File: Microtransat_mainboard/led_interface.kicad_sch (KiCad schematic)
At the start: 12 parts, among them J8 Conn_01x07

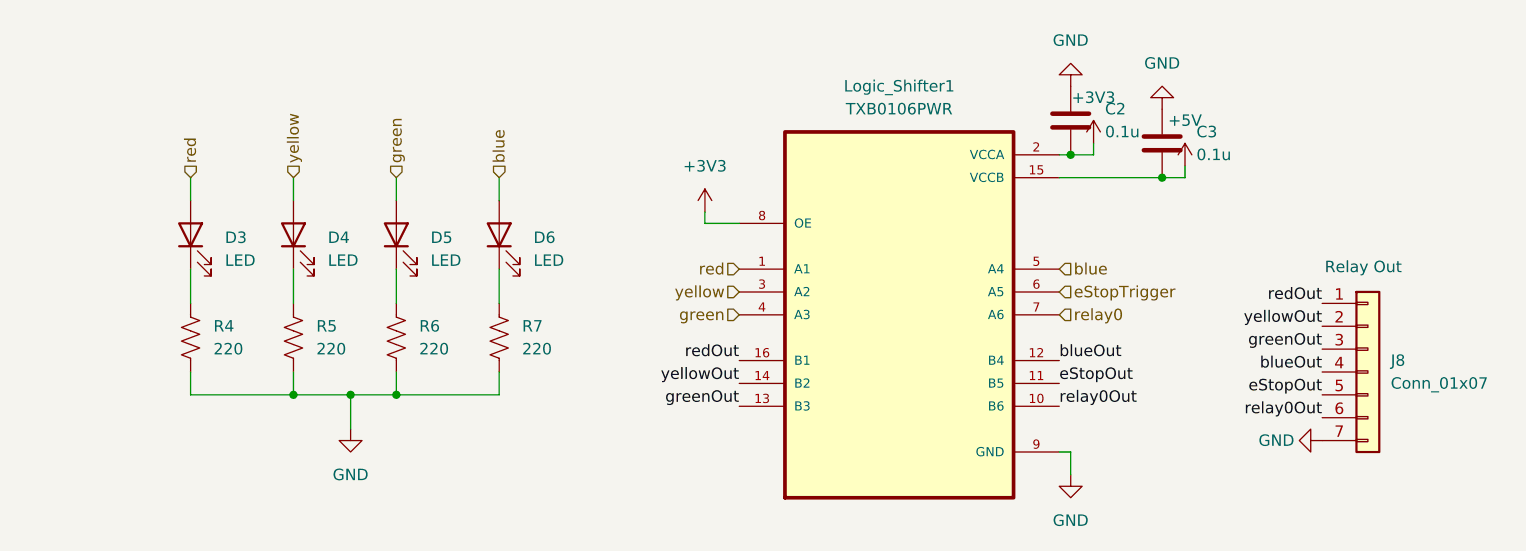
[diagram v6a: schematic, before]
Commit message: Some small changes to silkscreen and component numbers
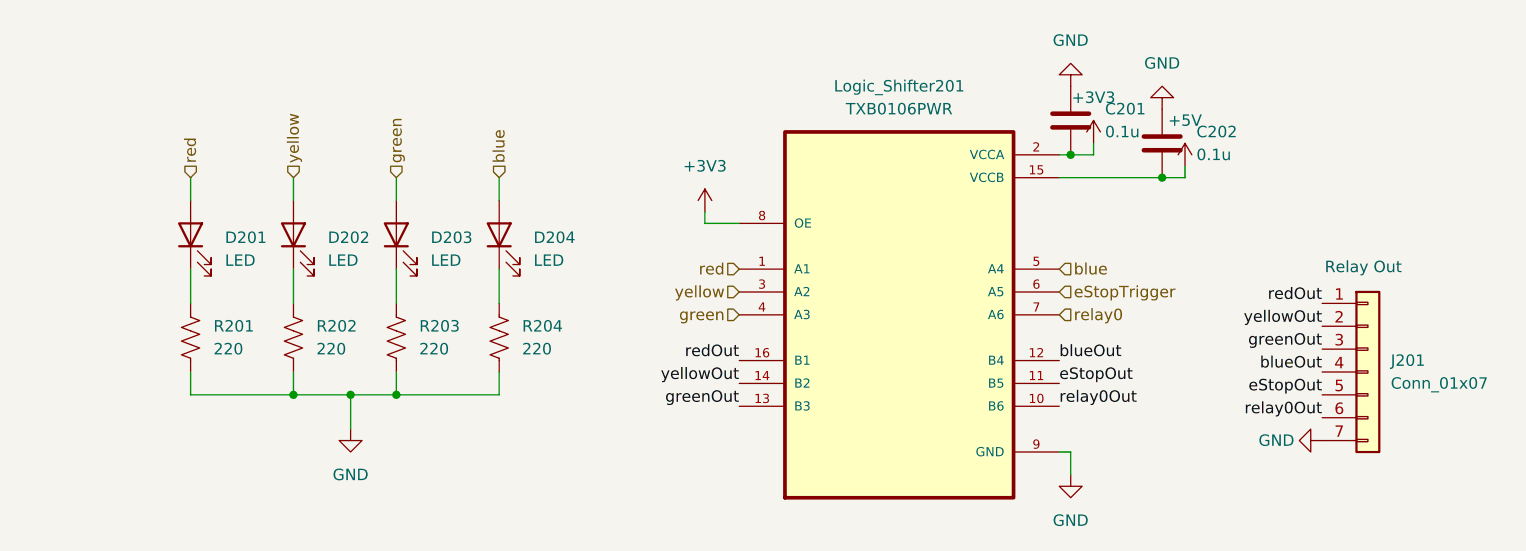
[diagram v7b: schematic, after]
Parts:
- renumbered C2 to C201, C3 to C202, D3 to D201, D4 to D202, D5 to D203, D6 to D204, J8 to J201, Logic_Shifter1 to Logic_Shifter201, R4 to R201, R5 to R202, R6 to R203, R7 to R204
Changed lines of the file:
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@@
 		(dnp no)
 		(fields_autoplaced yes)
-		(property "Reference" "R6"
+		(property "Reference" "R203"
 			(at 93.98 81.2799 0)
 			(effects
@@
 			(project "Microtransat_mainboard"
 				(path "/89914625-be83-416e-bb0d-b792f59b4aa6/2a723dab-0fe3-42a5-a32e-d625b3338ba9"
-					(reference "R6")
+					(reference "R203")
 					(unit 1)
 				)
@@
 		(dnp no)
 		(fields_autoplaced yes)
-		(property "Reference" "R4"
+		(property "Reference" "R201"
 			(at 71.12 81.2799 0)
 			(effects
@@
 			(project "Microtransat_mainboard"
 				(path "/89914625-be83-416e-bb0d-b792f59b4aa6/2a723dab-0fe3-42a5-a32e-d625b3338ba9"
-					(reference "R4")
+					(reference "R201")
 					(unit 1)
 				)
@@
 		(dnp no)
 		(fields_autoplaced yes)
-		(property "Reference" "#PWR031"
+		(property "Reference" "#PWR0205"
 			(at 168.91 64.77 0)
 			(effects
@@
 			(project "Microtransat_mainboard"
 				(path "/89914625-be83-416e-bb0d-b792f59b4aa6/2a723dab-0fe3-42a5-a32e-d625b3338ba9"
-					(reference "#PWR031")
+					(reference "#PWR0205")
 					(unit 1)
 				)
@@
 		(dnp no)
 		(fields_autoplaced yes)
-		(property "Reference" "R7"
+		(property "Reference" "R204"
 			(at 105.41 81.2799 0)
 			(effects
@@
 			(project "Microtransat_mainboard"
 				(path "/89914625-be83-416e-bb0d-b792f59b4aa6/2a723dab-0fe3-42a5-a32e-d625b3338ba9"
-					(reference "R7")
+					(reference "R204")
 					(unit 1)
 				)
@@
 		(dnp no)
 		(fields_autoplaced yes)
-		(property "Reference" "D4"
+		(property "Reference" "D202"
 			(at 83.82 71.4374 90)
 			(effects
@@
 			(project "Microtransat_mainboard"
 				(path "/89914625-be83-416e-bb0d-b792f59b4aa6/2a723dab-0fe3-42a5-a32e-d625b3338ba9"
-					(reference "D4")
+					(reference "D202")
 					(unit 1)
 				)
@@
 		(dnp no)
 		(fields_autoplaced yes)
-		(property "Reference" "#PWR033"
+		(property "Reference" "#PWR0207"
 			(at 179.07 67.31 0)
 			(effects
@@
 			(project "Microtransat_mainboard"
 				(path "/89914625-be83-416e-bb0d-b792f59b4aa6/2a723dab-0fe3-42a5-a32e-d625b3338ba9"
-					(reference "#PWR033")
+					(reference "#PWR0207")
 					(unit 1)
 				)
@@
 		(dnp no)
 		(fields_autoplaced yes)
-		(property "Reference" "J8"
+		(property "Reference" "J201"
 			(at 201.93 85.0899 0)
 			(effects
@@
 			(project ""
 				(path "/89914625-be83-416e-bb0d-b792f59b4aa6/2a723dab-0fe3-42a5-a32e-d625b3338ba9"
-					(reference "J8")
+					(reference "J201")
 					(unit 1)
 				)
@@
 		(dnp no)
 		(fields_autoplaced yes)
-		(property "Reference" "D6"
+		(property "Reference" "D204"
 			(at 106.68 71.4374 90)
 			(effects
@@
 			(project "Microtransat_mainboard"
 				(path "/89914625-be83-416e-bb0d-b792f59b4aa6/2a723dab-0fe3-42a5-a32e-d625b3338ba9"
-					(reference "D6")
+					(reference "D204")
 					(unit 1)
 				)
@@
 		(dnp no)
 		(fields_autoplaced yes)
-		(property "Reference" "#PWR029"
+		(property "Reference" "#PWR0203"
 			(at 166.37 48.26 0)
 			(effects
@@
 			(project "Microtransat_mainboard"
 				(path "/89914625-be83-416e-bb0d-b792f59b4aa6/2a723dab-0fe3-42a5-a32e-d625b3338ba9"
-					(reference "#PWR029")
+					(reference "#PWR0203")
 					(unit 1)
 				)
@@
 		(dnp no)
 		(fields_autoplaced yes)
-		(property "Reference" "#PWR030"
+		(property "Reference" "#PWR0204"
 			(at 166.37 104.14 0)
 			(effects
@@
 			(project "Microtransat_mainboard"
 				(path "/89914625-be83-416e-bb0d-b792f59b4aa6/2a723dab-0fe3-42a5-a32e-d625b3338ba9"
-					(reference "#PWR030")
+					(reference "#PWR0204")
 					(unit 1)
 				)
@@
 		(dnp no)
 		(fields_autoplaced yes)
-		(property "Reference" "#PWR032"
+		(property "Reference" "#PWR0206"
 			(at 176.53 50.8 0)
 			(effects
@@
 			(project "Microtransat_mainboard"
 				(path "/89914625-be83-416e-bb0d-b792f59b4aa6/2a723dab-0fe3-42a5-a32e-d625b3338ba9"
-					(reference "#PWR032")
+					(reference "#PWR0206")
 					(unit 1)
 				)
@@
 		(dnp no)
 		(fields_autoplaced yes)
-		(property "Reference" "D5"
+		(property "Reference" "D203"
 			(at 95.25 71.4374 90)
 			(effects
@@
 			(project "Microtransat_mainboard"
 				(path "/89914625-be83-416e-bb0d-b792f59b4aa6/2a723dab-0fe3-42a5-a32e-d625b3338ba9"
-					(reference "D5")
+					(reference "D203")
 					(unit 1)
 				)
@@
 		(dnp no)
 		(fields_autoplaced yes)
-		(property "Reference" "D3"
+		(property "Reference" "D201"
 			(at 72.39 71.4374 90)
 			(effects
@@
 			(project "Microtransat_mainboard"
 				(path "/89914625-be83-416e-bb0d-b792f59b4aa6/2a723dab-0fe3-42a5-a32e-d625b3338ba9"
-					(reference "D3")
+					(reference "D201")
 					(unit 1)
 				)
@@
 		(dnp no)
 		(fields_autoplaced yes)
-		(property "Reference" "#PWR027"
+		(property "Reference" "#PWR0201"
 			(at 86.36 99.06 0)
 			(effects
@@
 			(project "Microtransat_mainboard"
 				(path "/89914625-be83-416e-bb0d-b792f59b4aa6/2a723dab-0fe3-42a5-a32e-d625b3338ba9"
-					(reference "#PWR027")
+					(reference "#PWR0201")
 					(unit 1)
 				)
@@
 		(dnp no)
 		(fields_autoplaced yes)
-		(property "Reference" "Logic_Shifter1"
+		(property "Reference" "Logic_Shifter201"
 			(at 147.32 54.61 0)
 			(effects
@@
 			(project "Microtransat_mainboard"
 				(path "/89914625-be83-416e-bb0d-b792f59b4aa6/2a723dab-0fe3-42a5-a32e-d625b3338ba9"
-					(reference "Logic_Shifter1")
+					(reference "Logic_Shifter201")
 					(unit 1)
 				)
@@
 		(dnp no)
 		(fields_autoplaced yes)
-		(property "Reference" "C2"
+		(property "Reference" "C201"
 			(at 170.18 57.1499 0)
 			(effects
@@
 			(project ""
 				(path "/89914625-be83-416e-bb0d-b792f59b4aa6/2a723dab-0fe3-42a5-a32e-d625b3338ba9"
-					(reference "C2")
+					(reference "C201")
 					(unit 1)
 				)
@@
 		(dnp no)
 		(fields_autoplaced yes)
-		(property "Reference" "#PWR028"
+		(property "Reference" "#PWR0202"
 			(at 125.73 72.39 0)
 			(effects
@@
 			(project "Microtransat_mainboard"
 				(path "/89914625-be83-416e-bb0d-b792f59b4aa6/2a723dab-0fe3-42a5-a32e-d625b3338ba9"
-					(reference "#PWR028")
+					(reference "#PWR0202")
 					(unit 1)
 				)
@@
 		(on_board yes)
 		(dnp no)
-		(property "Reference" "#PWR034"
+		(property "Reference" "#PWR0208"
 			(at 187.96 93.98 0)
 			(effects
@@
 			(project "Microtransat_mainboard"
 				(path "/89914625-be83-416e-bb0d-b792f59b4aa6/2a723dab-0fe3-42a5-a32e-d625b3338ba9"
-					(reference "#PWR034")
+					(reference "#PWR0208")
 					(unit 1)
 				)
@@
 		(dnp no)
 		(fields_autoplaced yes)
-		(property "Reference" "C3"
+		(property "Reference" "C202"
 			(at 180.34 59.6899 0)
 			(effects
@@
 			(project "Microtransat_mainboard"
 				(path "/89914625-be83-416e-bb0d-b792f59b4aa6/2a723dab-0fe3-42a5-a32e-d625b3338ba9"
-					(reference "C3")
+					(reference "C202")
 					(unit 1)
 				)
@@
 		(dnp no)
 		(fields_autoplaced yes)
-		(property "Reference" "R5"
+		(property "Reference" "R202"
 			(at 82.55 81.2799 0)
 			(effects
@@
 			(project "Microtransat_mainboard"
 				(path "/89914625-be83-416e-bb0d-b792f59b4aa6/2a723dab-0fe3-42a5-a32e-d625b3338ba9"
-					(reference "R5")
-					(unit 1)
-				)
+					(reference "R202")
+					(unit 1)
+				)

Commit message: Fixed changes from design review
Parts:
- removed J201: Conn_01x07, Connector_PinSocket_2.54mm:PinSocket_1x07_P2.54mm_Vertical, symbol Connector_Generic:Conn_01x07
- added D1, D2: LED, LED_SMD:LED_1206_3216Metric_Pad1.42x1.75mm_HandSolder, symbol Device:LED
- added J1: Conn_01x06, Connector_JST:JST_XH_B6B-XH-A_1x06_P2.50mm_Vertical, symbol Connector_Generic:Conn_01x06
- added J2: Conn_01x02, Connector_JST:JST_XH_B2B-XH-A_1x02_P2.50mm_Vertical, symbol Connector_Generic:Conn_01x02
- added R1, R2: 220, Resistor_SMD:R_1206_3216Metric_Pad1.30x1.75mm_HandSolder, symbol Device:R_US
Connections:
- net +5V: now also J2.1 (Pin_1)
- net GND: now also J2.2 (Pin_2), R1.2, R2.2
- net blueOut: now also J1.4 (Pin_4)
- net eStopOut: now also J1.5 (Pin_5)
- net eStopTrigger: now also D1.2 (A)
- net greenOut: now also J1.3 (Pin_3)
- net redOut: now also J1.1 (Pin_1)
- net relay0: now also D2.2 (A)
- net relay0Out: now also J1.6 (Pin_6)
- net yellowOut: now also J1.2 (Pin_2)
- new net: D1.1 (K), R1.1
- new net: D2.1 (K), R2.1
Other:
- moved on the sheet: D201, D202, D203, D204, R201, R202, R203, R204
